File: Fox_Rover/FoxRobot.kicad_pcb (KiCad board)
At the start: 4 copper layers, 33 parts, among them J1 Screw_Terminal_01x02, J2 XT60-M_Green, J3 XT60-M_Red, J4 Screw_Terminal_01x02, J5 Conn_02x10_Odd_Even, J6 Screw_Terminal_01x02, K1 40.52.7.012.0000, K2 G2RK-1_12DC, K3 ADJH23005, K4 ADJH23005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

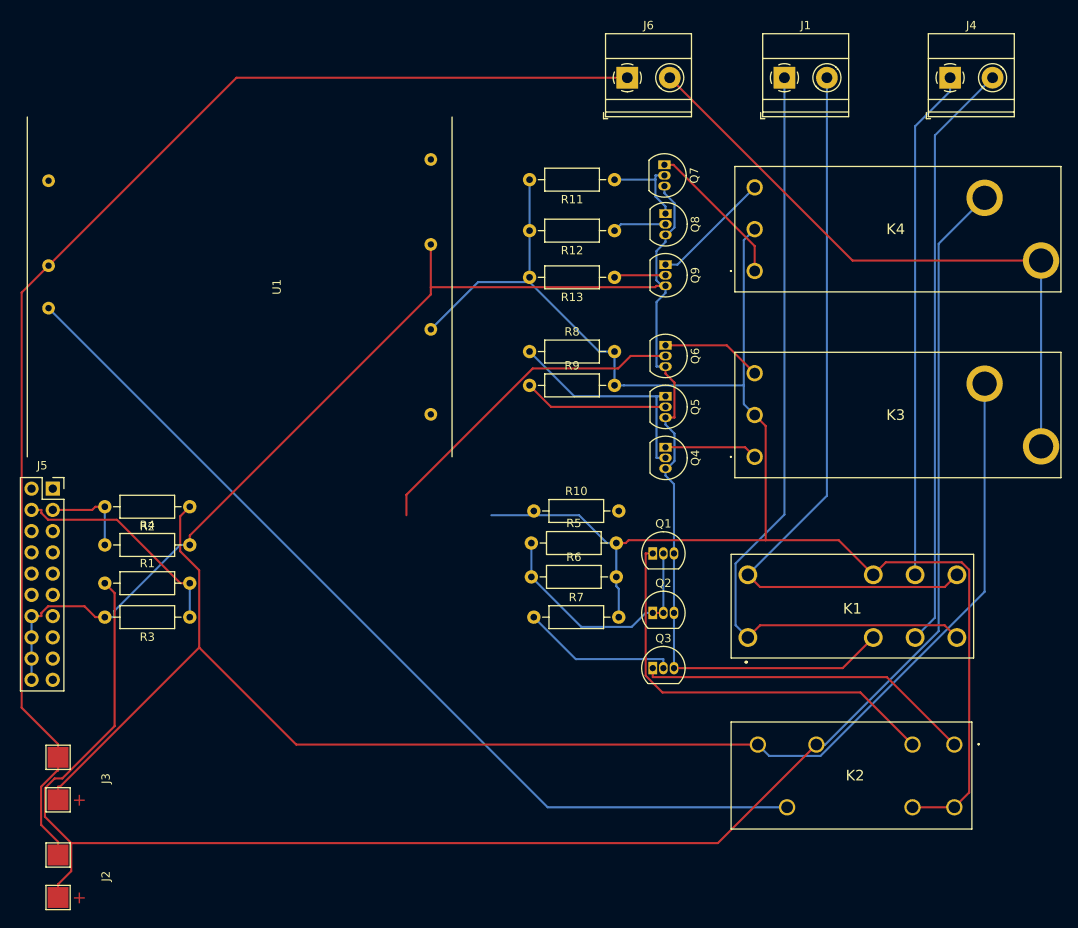
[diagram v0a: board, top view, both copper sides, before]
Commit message: Added an extra header output to the schematics and started initial PCB designs
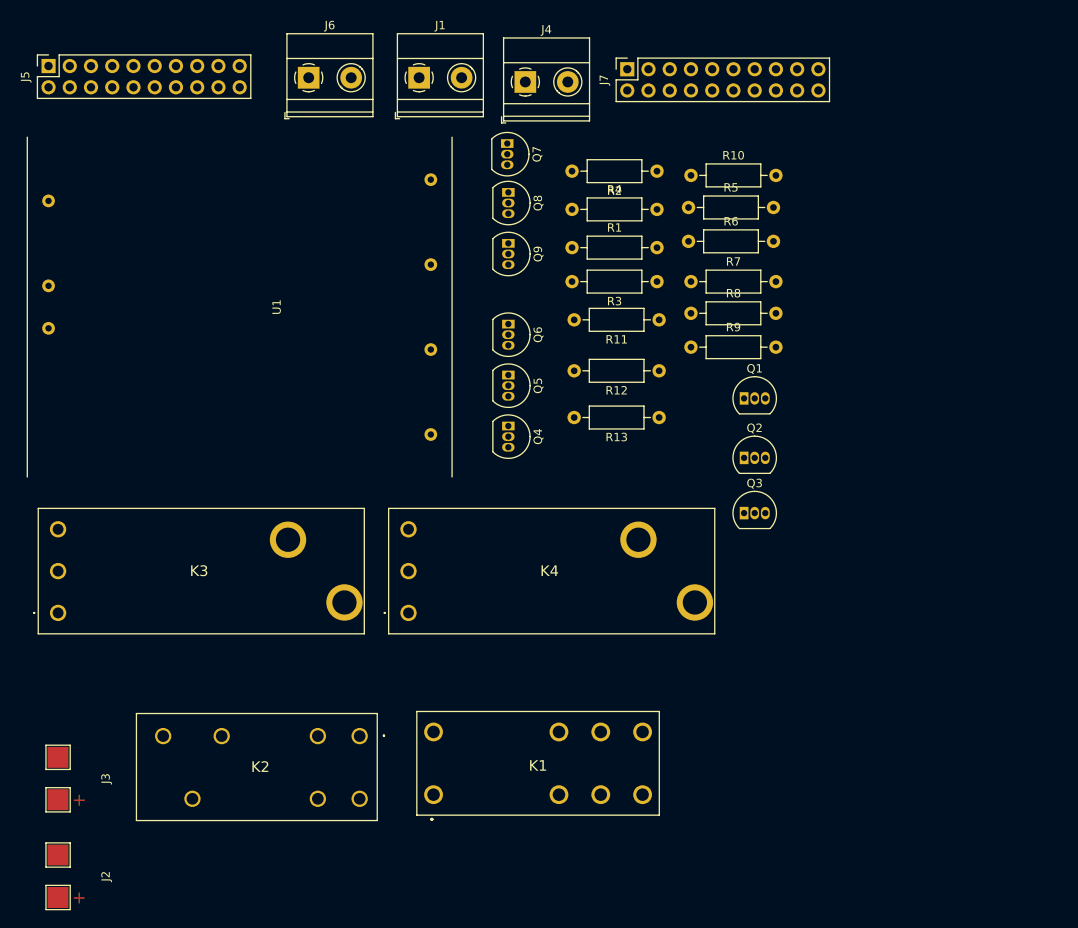
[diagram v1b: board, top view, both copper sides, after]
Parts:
- added J7: Conn_02x10_Odd_Even, Connector_PinSocket_2.54mm:PinSocket_2x10_P2.54mm_Vertical, F.Cu at (86.4, 17.8)
- moved K3 85.4 mm to (18.3, 82.8)
- moved K2 71.1 mm to (54.4, 97.5)
- moved R1 68.8 mm to (79.8, 39.1)
- moved R2 68.8 mm to (89.9, 30.0)
- moved R3 68.8 mm to (89.9, 43.2)
- moved R4 68.8 mm to (79.8, 34.5)
- moved K4 58.2 mm to (60.2, 82.8)
- moved J4 50.8 mm to (74.2, 19.3)
- moved J5 50.5 mm to (17.1, 17.4), turned to 90 degrees
- moved R6 44.3 mm to (93.7, 38.4)
- moved R7 44.3 mm to (94.0, 43.2)
- moved R10 44.3 mm to (94.0, 30.5)
- moved R5 44.3 mm to (93.7, 34.3)
- moved J1 43.7 mm to (61.5, 18.8)
- moved K1 42.0 mm to (75.7, 101.1)
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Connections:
- J5 pad 5: (no net) -> Net-(J2-Pad2)
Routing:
- net Net-(J2-Pad2): track 212.4 -> 0.00 mm
- net +5V: track 202.8 -> 0.00 mm
- net GND: track 197.7 -> 0.00 mm
- net Net-(J3-Pad2): track 175.9 -> 0.00 mm
- net Net-(J2-Pad1): track 153.9 -> 0.00 mm
- net Net-(K2-Pad5): track 113.1 -> 0.00 mm
- net Net-(J1-Pad1): track 96.2 -> 0.00 mm
- net Net-(J1-Pad2): track 89.6 -> 0.00 mm
- net Net-(J6-Pad2): track 75.7 -> 0.00 mm
- net Net-(J4-Pad2): track 70.8 -> 0.00 mm
- net Net-(J4-Pad1): track 61.2 -> 0.00 mm
- net Net-(K2-Pad2): track 50.8 -> 0.00 mm
- net Net-(K2-Pad1): track 40.5 -> 0.00 mm
- net Net-(Q6-Pad2): track 40.3 -> 0.00 mm
- net Net-(Q1-Pad2): track 30.1 -> 0.00 mm
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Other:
- copper layers 4 -> 2
- net class Batt added: clearance 0.4, trace_width 2.8, via_dia 0.8, via_drill 0.4
- net class Default: clearance 0.2 -> 0.3
- rule trace_clearance: 0.2 -> 0.3

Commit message: PCB design suitable
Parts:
- added REF**: MountingHole_3.2mm_M3_DIN965_Pad, MountingHole:MountingHole_3.2mm_M3_DIN965_Pad, F.Cu at (21.6, 24.1)
- added REF**: MountingHole_3.2mm_M3_DIN965_Pad, MountingHole:MountingHole_3.2mm_M3_DIN965_Pad, F.Cu at (106.7, 25.4)
- added REF**: MountingHole_3.2mm_M3_DIN965_Pad, MountingHole:MountingHole_3.2mm_M3_DIN965_Pad, F.Cu at (105.4, 119.4)
- added REF**: MountingHole_3.2mm_M3_DIN965_Pad, MountingHole:MountingHole_3.2mm_M3_DIN965_Pad, F.Cu at (33.0, 119.4)
- moved Q6 5.68 mm to (74.7, 53.3)
- moved Q9 5.68 mm to (74.7, 43.7)
- moved R4 5.68 mm to (82.3, 39.6)
- moved K1 5.68 mm to (78.2, 106.2)
- moved Q1 5.68 mm to (102.9, 62.2)
- moved Q2 5.68 mm to (102.9, 69.3)
- moved Q3 5.68 mm to (102.9, 75.9)
- moved Q4 5.68 mm to (74.7, 65.5)
- moved Q5 5.68 mm to (74.7, 59.4)
- moved Q7 5.68 mm to (74.5, 31.8)
- moved Q8 5.68 mm to (74.7, 37.6)
- moved R1 5.68 mm to (82.3, 44.2)
- moved R13 5.68 mm to (92.7, 64.5)
- moved R2 5.68 mm to (92.5, 35.1)
- moved R3 5.68 mm to (92.5, 48.3)
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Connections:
- J5 pad 1: (no net) -> /A1
- J5 pad 10: (no net) -> /A10
- J5 pad 11: (no net) -> /A11
- J5 pad 12: (no net) -> /A12
- J5 pad 13: (no net) -> /A13
- J5 pad 15: (no net) -> /A15
- J5 pad 17: (no net) -> /A17
- J5 pad 19: (no net) -> /A19
- J5 pad 2: (no net) -> /A2
- J5 pad 3: Net-(J5-Pad3) -> /A3
- J5 pad 4: Net-(J5-Pad4) -> /A4
- J5 pad 5: Net-(J2-Pad2) -> /A5
- J5 pad 6: (no net) -> /A6
- J5 pad 7: (no net) -> /A7
- J5 pad 8: (no net) -> /A8
- J5 pad 9: (no net) -> /A9
- J7 pad 1: (no net) -> /A1
- J7 pad 10: (no net) -> /A10
- J7 pad 11: (no net) -> /A11
- J7 pad 12: (no net) -> /A12
- J7 pad 13: (no net) -> /A13
- J7 pad 14: (no net) -> GND
- J7 pad 15: (no net) -> /A15
- J7 pad 16: (no net) -> GND
- J7 pad 17: (no net) -> /A17
- J7 pad 18: (no net) -> GND
- J7 pad 19: (no net) -> /A19
- J7 pad 2: (no net) -> /A2
- J7 pad 20: (no net) -> GND
- J7 pad 3: (no net) -> /A3
- J7 pad 4: (no net) -> /A4
- J7 pad 5: (no net) -> /A5
- J7 pad 6: (no net) -> /A6
- J7 pad 7: (no net) -> /A7
- J7 pad 8: (no net) -> /A8
- J7 pad 9: (no net) -> /A9
- R1 pad 2: Net-(J5-Pad4) -> /A4
- R2 pad 2: Net-(J5-Pad3) -> /A3
- R3 pad 1: Net-(J5-Pad4) -> /A4
- R4 pad 1: Net-(J5-Pad3) -> /A3
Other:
- net class Default: trace_width 0.25 -> 0.3
- board text added: "Rover_ElectronicsV1.0"

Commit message: Adjusted for mounting platforms
Adjust sizing for lower pricing
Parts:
- removed REF** (x4): MountingHole_3.2mm_M3_DIN965_Pad, MountingHole:MountingHole_3.2mm_M3_DIN965_Pad
- added H1: MountingHole, MountingHole:MountingHole_3.2mm_M3_ISO7380_Pad_TopBottom, F.Cu at (19.1, 24.1)
- added H2: MountingHole, MountingHole:MountingHole_3.2mm_M3_ISO7380_Pad_TopBottom, F.Cu at (100.9, 28.2)
- added H3: MountingHole, MountingHole:MountingHole_3.2mm_M3_ISO7380_Pad_TopBottom, F.Cu at (33.0, 119.4)
- added H4: MountingHole, MountingHole:MountingHole_3.2mm_M3_ISO7380_Pad_TopBottom, F.Cu at (109.2, 119.4)
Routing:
- net GND: track 0.00 -> 298.0 mm
- net +5V: track 0.00 -> 254.0 mm
- net Net-(J2-Pad2): track 0.00 -> 154.5 mm, vias 0 -> 1
- net Net-(J3-Pad2): track 0.00 -> 121.6 mm
- net Net-(J1-Pad1): track 0.00 -> 120.2 mm
- net Net-(J2-Pad1): track 0.00 -> 118.6 mm
- net Net-(J6-Pad2): track 0.00 -> 113.2 mm
- net /A3: track 0.00 -> 111.6 mm
- net Net-(J1-Pad2): track 0.00 -> 110.8 mm
- net /A4: track 0.00 -> 102.5 mm, vias 0 -> 1
- net Net-(J4-Pad2): track 0.00 -> 96.8 mm
- net Net-(K2-Pad2): track 0.00 -> 88.2 mm
- net Net-(J4-Pad1): track 0.00 -> 86.8 mm
- net /A2: track 0.00 -> 79.1 mm, vias 0 -> 1
- net /A1: track 0.00 -> 76.1 mm, vias 0 -> 1
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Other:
- board outline added: 102.9 x 116.8 mm
- board text added: "24V+"

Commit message: Added Schem
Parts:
- moved H4 105.7 mm to (205.7, 162.6)
- moved J4 105.7 mm to (173.2, 62.2)
- moved K1 105.7 mm to (174.8, 149.4)
- moved K4 105.7 mm to (159.3, 131.1)
- moved R5 105.7 mm to (192.7, 82.6)
- moved R6 105.7 mm to (192.7, 86.6)
- moved R8 105.7 mm to (193.0, 95.2)
- moved R9 105.7 mm to (193.0, 99.3)
- moved H1 105.7 mm to (115.6, 67.3)
- moved H2 105.7 mm to (197.4, 71.3)
- moved J1 105.7 mm to (160.5, 62.2)
- moved J2 105.7 mm to (117.3, 162.6)
- moved J3 105.7 mm to (117.3, 150.9)
- moved J5 105.7 mm to (116.2, 58.4)
- moved J6 105.7 mm to (147.3, 62.2)
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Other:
- board outline removed

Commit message: Added the filter capacitor and coil.
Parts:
- added C1: 330uF, Capacitor_THT:C_Disc_D7.5mm_W2.5mm_P5.00mm, F.Cu at (157.9, 161.5)
- added C2: 100uF, Capacitor_THT:C_Disc_D7.5mm_W2.5mm_P5.00mm, F.Cu at (168.9, 161.3)
- added L1: L, Inductor_THT:L_Radial_D10.0mm_P5.00mm_Fastron_07M, F.Cu at (144.8, 163.8)
- R10, R11, R12, R13, R5, R6, R7, R8, R9: value R -> 10k
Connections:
- J2 pad 1: Net-(J2-Pad1) -> GND
- J3 pad 1: Net-(J2-Pad1) -> GND
- J6 pad 1: Net-(J2-Pad1) -> GND
- K2 pad 5: Net-(K2-Pad5) -> Net-(C1-Pad1)
- Q2 pad 2: Net-(Q1-Pad2) -> Net-(Q2-Pad2)
- R6 pad 1: Net-(Q1-Pad2) -> Net-(Q2-Pad2)
- U1 pad 3: Net-(J2-Pad1) -> GND
- U1 pad 4: Net-(K2-Pad5) -> Net-(C2-Pad1)
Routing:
- net Net-(J2-Pad1): track 118.6 -> 0.00 mm
- net GND: track 298.0 -> 415.3 mm
- net Net-(C2-Pad1): track 0.00 -> 105.6 mm
- net Net-(K2-Pad5): track 63.4 -> 0.00 mm
- net Net-(Q9-Pad2): track 64.4 -> 31.6 mm, vias 0 -> 1
- net Net-(Q2-Pad2): track 0.00 -> 31.1 mm
- net Net-(C1-Pad1): track 0.00 -> 29.7 mm
- net Net-(Q8-Pad2): track 56.3 -> 29.4 mm, vias 0 -> 1
- net Net-(K2-Pad2): track 88.2 -> 67.7 mm
- net /A2: track 79.1 -> 72.3 mm
- net Net-(K2-Pad1): track 64.9 -> 58.3 mm
- net Net-(J1-Pad1): track 120.2 -> 125.6 mm
- net Net-(J6-Pad2): track 113.2 -> 118.5 mm, vias 0 -> 1
- net Net-(Q5-Pad2): track 26.9 -> 31.9 mm
- net Net-(J1-Pad2): track 110.8 -> 115.1 mm
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
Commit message: Adjusted libraries pathing
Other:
- board text added: "Adjusted Version"
